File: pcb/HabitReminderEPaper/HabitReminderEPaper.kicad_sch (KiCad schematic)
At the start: 19 parts, among them Q1 Si1308EDL

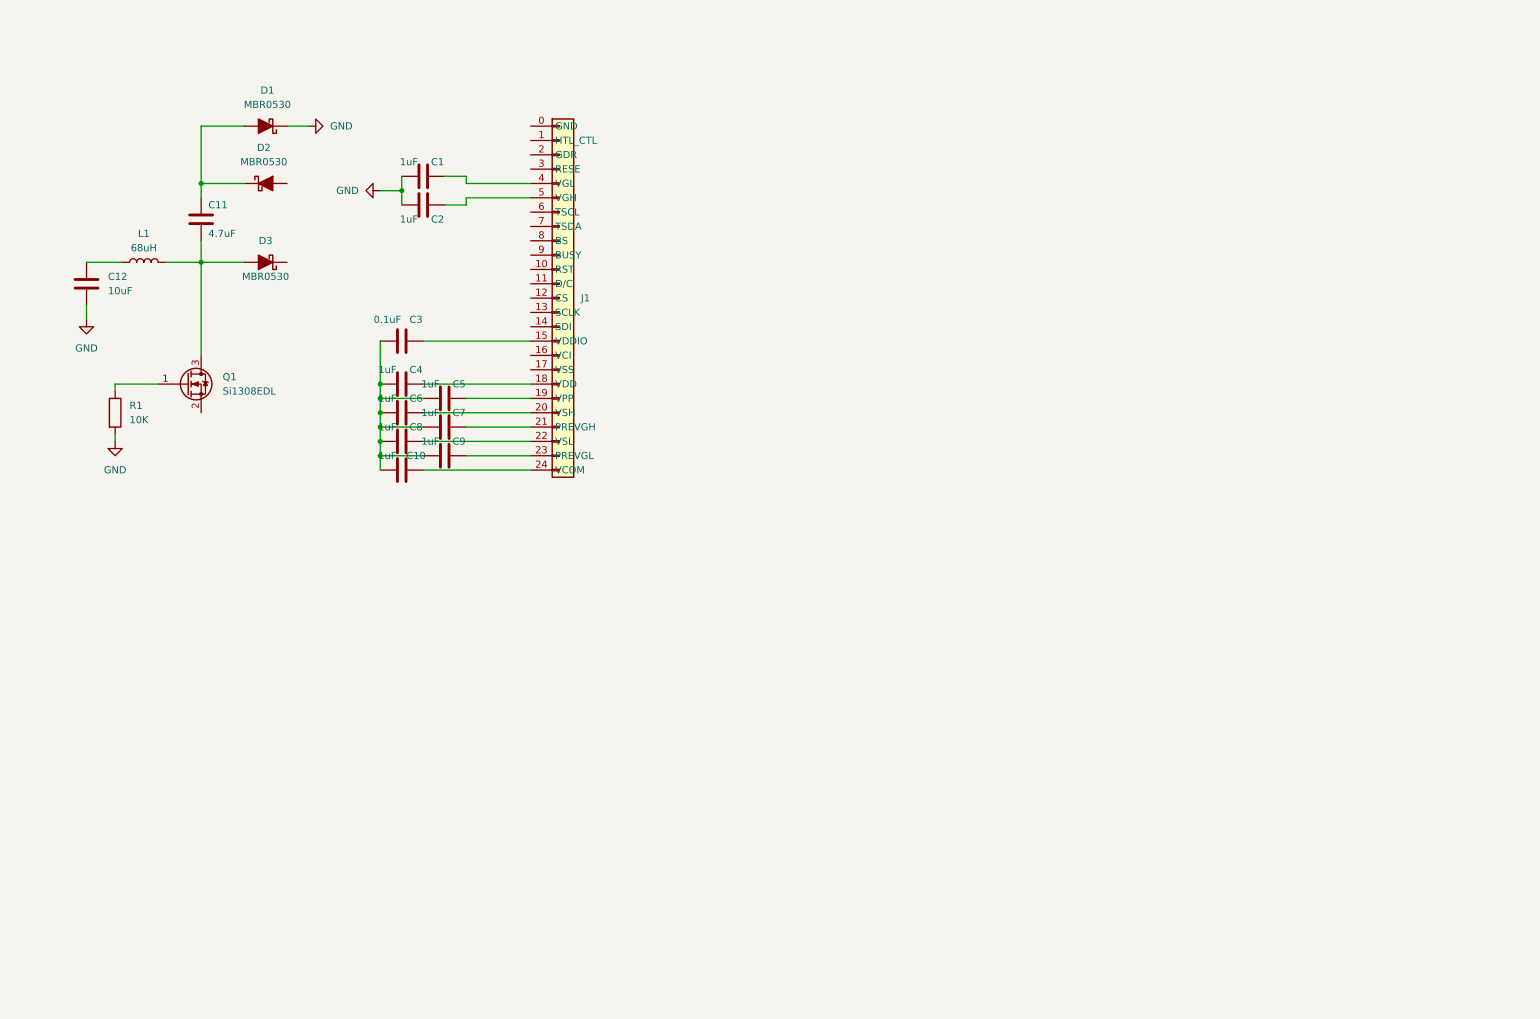
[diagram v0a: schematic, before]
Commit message: Epaper initial prototype. Still needs main user buttons footprints
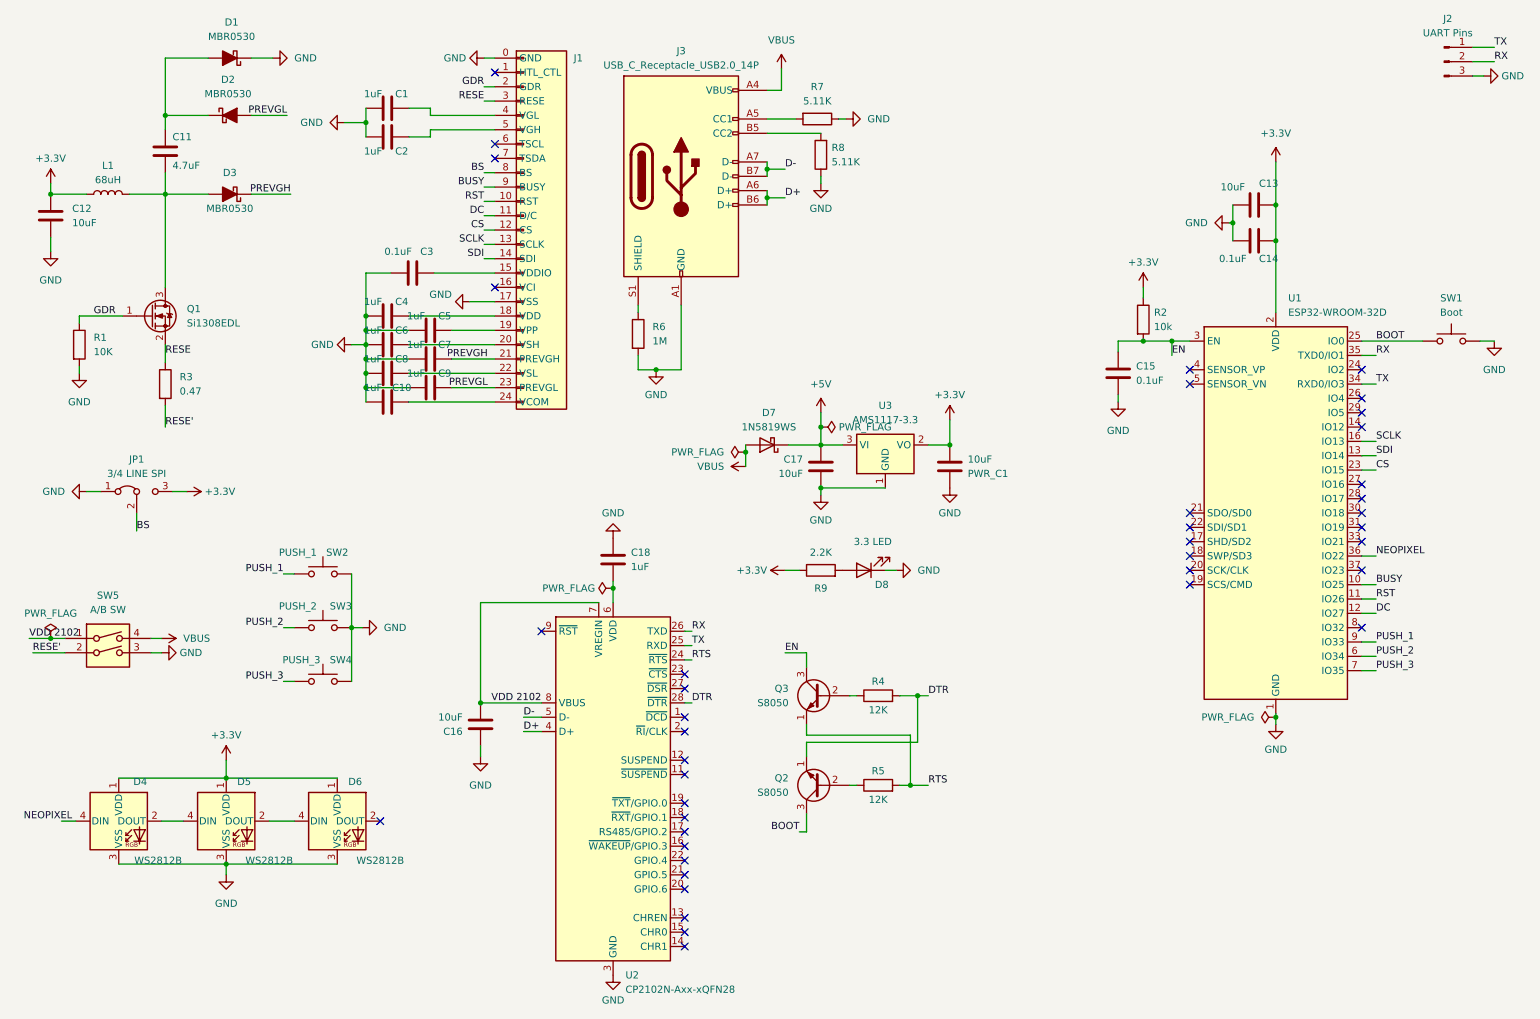
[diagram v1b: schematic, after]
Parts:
- added C13, C16, C17: 10uF, Capacitor_SMD:C_0201_0603Metric, symbol Device:C
- added C14, C15: 0.1uF, Capacitor_SMD:C_0201_0603Metric, symbol Device:C
- added C18: 1uF, Capacitor_SMD:C_0201_0603Metric, symbol Device:C
- added D4, D5, D6: WS2812B, LED_SMD:LED_WS2812B_PLCC4_5.0x5.0mm_P3.2mm, symbol LED:WS2812B
- added D7: 1N5819WS, Diode_SMD:D_SOD-323, symbol Diode:1N5819WS
- added D8: 3.3 LED, Diode_SMD:D_0201_0603Metric, symbol Device:LED
- added J2: UART Pins, Connector_PinHeader_2.54mm:PinHeader_1x03_P2.54mm_Vertical, symbol Connector:Conn_01x03_Pin
- added J3: USB_C_Receptacle_USB2.0_14P, Connector_USB:USB_C_Receptacle_G-Switch_GT-USB-7010ASV, symbol Connector:USB_C_Receptacle_USB2.0_14P
- added JP1: 3/4 LINE SPI, PCM_Jumper_AKL:Jumper_P2.54mm_D0.7mm, symbol Jumper:Jumper_3_Bridged12
- added PWR_C1: 10uF, Capacitor_SMD:C_0402_1005Metric, symbol Device:C
- added Q2, Q3: S8050, Package_TO_SOT_THT:TO-92_Inline, symbol Transistor_BJT:S8050
- added R2: 10k, PCM_Resistor_SMD_AKL:R_0201_0603Metric, symbol Device:R
- added R3: 0.47, PCM_Resistor_SMD_AKL:R_0201_0603Metric, symbol Device:R
- added R4, R5: 12K, PCM_Resistor_SMD_AKL:R_0201_0603Metric, symbol Device:R
- added R6: 1M, PCM_Resistor_SMD_AKL:R_0201_0603Metric, symbol Device:R
- added R7, R8: 5.11K, PCM_Resistor_SMD_AKL:R_0201_0603Metric, symbol Device:R
- added R9: 2.2K, PCM_Resistor_SMD_AKL:R_0201_0603Metric, symbol Device:R
- added SW1: Boot, Button_Switch_SMD:SW_Push_1P1T_NO_6x6mm_H9.5mm, symbol Switch:SW_Push
- added SW2: PUSH_1, symbol Switch:SW_Push
- added SW3: PUSH_2, symbol Switch:SW_Push
- added SW4: PUSH_3, symbol Switch:SW_Push
- added SW5: A/B SW, symbol Switch:SW_DIP_x02
- added U1: ESP32-WROOM-32D, RF_Module:ESP32-WROOM-32D, symbol RF_Module:ESP32-WROOM-32D
- added U2: CP2102N-Axx-xQFN28, Package_DFN_QFN:QFN-28-1EP_5x5mm_P0.5mm_EP3.35x3.35mm, symbol Interface_USB:CP2102N-Axx-xQFN28
- added U3: AMS1117-3.3, Package_TO_SOT_SMD:SOT-223-3_TabPin2, symbol Regulator_Linear:AMS1117-3.3
- C1, C10, C11, C12, C2, C3, C4, C5, C6, C7, C8, C9: footprint (none) -> Capacitor_SMD:C_0201_0603Metric
- D1, D2, D3: footprint Diode_SMD_AKL:D_SOD-123 -> Diode_SMD:D_SOD-123
- J1: footprint (none) -> Connector_FFC-FPC:Jushuo_AFC07-S24FCA-00_1x24-1MP_P0.50_Horizontal
- L1: footprint (none) -> Inductor_SMD:L_0201_0603Metric
- R1: footprint (none) -> PCM_Resistor_SMD_AKL:R_0201_0603Metric
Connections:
- net GND: now also C10.1, C3.1, C4.1, C5.1, C6.1, C7.1, C8.1, C9.1, J1.0 (GND), J1.17 (VSS), C13.1, C14.1, C15.1, C16.1, C17.1, C18.1, D4.3 (VSS), D5.3 (VSS), D6.3 (VSS), D8.1 (K), J2.3 (Pin_3), J3.A1 (GND), J3.A12 (GND), J3.B1 (GND), J3.B12 (GND), JP1.1 (A), PWR_C1.2, R6.2, R7.1, R8.1, SW1.2, SW2.2, SW3.2, SW4.2, SW5.3, U1.1 (GND), U1.15 (GND), U1.38 (GND), U1.39 (GND), U2.29 (GND), U2.3 (GND), U3.1 (GND)
- net PREVGH: now reaches D3.1 (K)
- net PREVGH: now also C7.2, J1.21 (PREVGH)
- net PREVGL: now reaches D2.2 (A)
- net PREVGL: now also C9.2, J1.23 (PREVGL)
- net RST: now reaches J1.10 (RST)
- net RST: now also U1.11 (IO26)
- net DC: now reaches J1.11 (D/C)
- net DC: now also U1.12 (IO27)
- net CS: now reaches J1.12 (CS)
- net CS: now also U1.23 (IO15)
- net SCLK: now reaches J1.13 (SCLK)
- net SCLK: now also U1.16 (IO13)
- net SDI: now reaches J1.14 (SDI)
- net SDI: now also U1.13 (IO14)
- net GDR: now reaches J1.2 (GDR)
- net GDR: now also Q1.1 (G), R1.1
- net RESE: now reaches J1.3 (RESE)
- net RESE: now also Q1.2 (S), R3.1
- net BS: now reaches J1.8 (BS)
- net BS: now also JP1.2 (C)
- net BUSY: now reaches J1.9 (BUSY)
- net BUSY: now also U1.10 (IO25)
- net +3.3V: now reaches C12.1, L1.1
- net +3.3V: now also C13.2, C14.2, D4.1 (VDD), D5.1 (VDD), D6.1 (VDD), JP1.3 (B), PWR_C1.1, R2.1, R9.1, U1.2 (VDD), U3.2 (VO)
- new net: J3.B5 (CC2), R8.2
- new net: D5.2 (DOUT), D6.4 (DIN)
- new net: D4.2 (DOUT), D5.4 (DIN)
- new net: Q3.2 (B), R4.1
- new net: D8.2 (A), R9.2
- new net: C18.2, U2.6 (VDD)
- new net: J3.S1 (SHIELD), R6.1
- new net: Q2.2 (B), R5.1
- new net: J3.A5 (CC1), R7.2
- new net +5V: C17.2, D7.1 (K), U3.3 (VI)
- new net BOOT: Q2.3 (C), SW1.1, U1.25 (IO0)
- new net D+: J3.A6 (D+), J3.B6 (D+), U2.4 (D+)
- new net D-: J3.A7 (D-), J3.B7 (D-), U2.5 (D-)
- new net DTR: Q2.1 (E), R4.2, U2.28 (~{DTR})
- new net EN: C15.2, Q3.3 (C), R2.2, U1.3 (EN)
- new net NEOPIXEL: D4.4 (DIN), U1.36 (IO22)
- new net PUSH_1: SW2.1, U1.9 (IO33)
- new net PUSH_2: SW3.1, U1.6 (IO34)
- new net PUSH_3: SW4.1, U1.7 (IO35)
- new net RESE': R3.2, SW5.2
- new net RTS: Q3.1 (E), R5.2, U2.24 (~{RTS})
- new net RX: J2.2 (Pin_2), U1.35 (TXD0/IO1), U2.26 (TXD)
- new net TX: J2.1 (Pin_1), U1.34 (RXD0/IO3), U2.25 (RXD)
- new net VBUS: D7.2 (A), J3.A4 (VBUS), J3.A9 (VBUS), J3.B4 (VBUS), J3.B9 (VBUS), SW5.4
- new net VDD 2102: C16.2, SW5.1, U2.7 (VREGIN), U2.8 (VBUS)
- no-connect marks 0 -> 41
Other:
- moved on the sheet: C1, C10, C11, C12, C2, C3, C4, C5, C6, C7, C8, C9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

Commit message: inital E-Paper prototype, OLED inital board finished
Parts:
- SW1: footprint Button_Switch_SMD:SW_Push_1P1T_NO_6x6mm_H9.5mm -> Button_Switch_SMD:SW_Push_SPST_NO_Alps_SKRK
- SW2, SW3, SW4: footprint (none) -> Button_Switch_THT:SW_PUSH_6mm
- SW5: footprint (none) -> Button_Switch_THT:SW_DIP_SPSTx02_Slide_6.7x6.64mm_W7.62mm_P2.54mm_LowProfile
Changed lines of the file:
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@@
       (effects (font (size 1.27 1.27)))
     )
-    (property "Footprint" "" (at 68.58 127.635 0)
+    (property "Footprint" "Button_Switch_THT:SW_PUSH_6mm" (at 68.58 127.635 0)
       (effects (font (size 1.27 1.27)) hide)
     )
@@
       (effects (font (size 1.27 1.27)))
     )
-    (property "Footprint" "" (at 68.58 108.585 0)
+    (property "Footprint" "Button_Switch_THT:SW_PUSH_6mm" (at 68.58 108.585 0)
       (effects (font (size 1.27 1.27)) hide)
     )
@@
       (effects (font (size 1.27 1.27)))
     )
-    (property "Footprint" "" (at 68.58 118.11 0)
+    (property "Footprint" "Button_Switch_THT:SW_PUSH_6mm" (at 68.58 118.11 0)
       (effects (font (size 1.27 1.27)) hide)
     )
@@
       (effects (font (size 1.27 1.27)))
     )
-    (property "Footprint" "Button_Switch_SMD:SW_Push_1P1T_NO_6x6mm_H9.5mm" (at 268.605 67.31 0)
+    (property "Footprint" "Button_Switch_SMD:SW_Push_SPST_NO_Alps_SKRK" (at 268.605 67.31 0)
       (effects (font (size 1.27 1.27)) hide)
     )
@@
       (effects (font (size 1.27 1.27)))
     )
-    (property "Footprint" "" (at 30.48 127.635 0)
-      (effects (font (size 1.27 1.27)) hide)
-    )
+    (property "Footprint" "Button_Switch_THT:SW_DIP_SPSTx02_Slide_6.7x6.64mm_W7.62mm_P2.54mm_LowProfile" (at 30.48 127.635 0)
+      (effects (font (size 1.27 1.27)) hide)
+    )
